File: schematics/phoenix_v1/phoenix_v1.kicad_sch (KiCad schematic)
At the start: 18 parts, among them J1 Screw_Terminal_01x02, J2 Conn_01x09_Socket, SW1 RotaryEncoder_Switch, U1 HHG1D-1, U2 ESP32-S3-DevKitC, U3 NHD-C0220BIZ

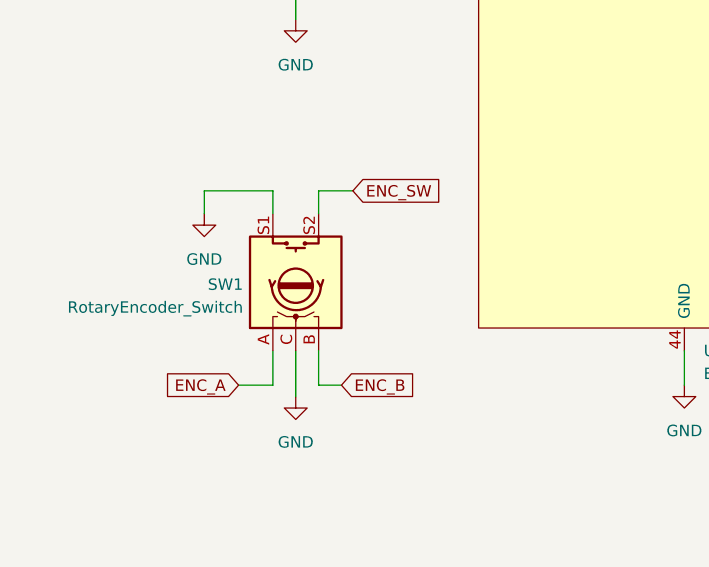
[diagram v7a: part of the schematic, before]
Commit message: fix encoder footprint and label mismatch
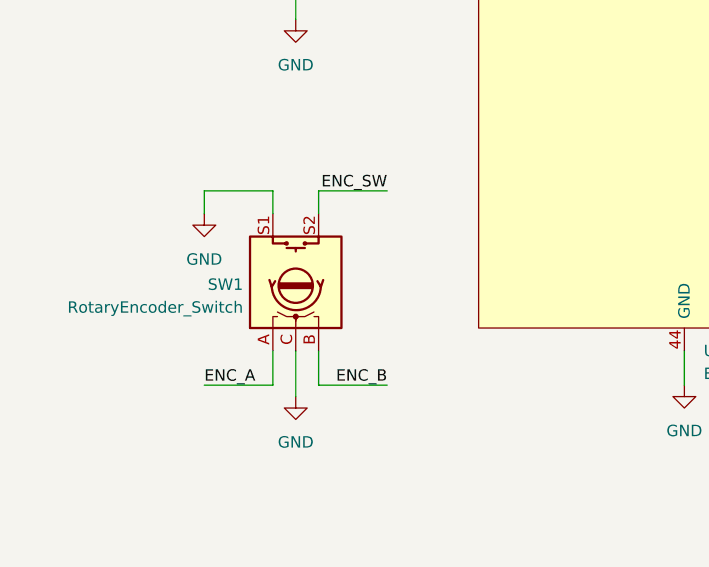
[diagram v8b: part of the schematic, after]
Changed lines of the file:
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@@
-	(wire
-		(pts
-			(xy 48.26 140.97) (xy 44.45 140.97)
-		)
-		(stroke
-			(width 0)
-			(type default)
-		)
-	)
 	(wire
 		(pts
@@
 	(wire
 		(pts
-			(xy 53.34 119.38) (xy 57.15 119.38)
+			(xy 53.34 119.38) (xy 60.96 119.38)
 		)
 		(stroke
@@
 	(wire
 		(pts
-			(xy 53.34 140.97) (xy 55.88 140.97)
+			(xy 53.34 140.97) (xy 60.96 140.97)
 		)
 		(stroke
@@
 		(pts
 			(xy 119.38 132.08) (xy 123.19 132.08)
+		)
+		(stroke
+			(width 0)
+			(type default)
+		)
+	)
+	(wire
+		(pts
+			(xy 40.64 140.97) (xy 48.26 140.97)
 		)
 		(stroke
@@
 		)
 	)
+	(label "ENC_SW"
+		(at 60.96 119.38 180)
+		(effects
+			(font
+				(size 1.27 1.27)
+			)
+			(justify right bottom)
+		)
+	)
 	(label "SCL"
 		(at 146.05 41.91 0)
@@
 		)
 	)
+	(label "ENC_B"
+		(at 60.96 140.97 180)
+		(effects
+			(font
+				(size 1.27 1.27)
+			)
+			(justify right bottom)
+		)
+	)
 	(label "~{FAULT}"
 		(at 116.84 160.02 0)
@@
 		)
 	)
-	(global_label "ENC_SW"
-		(shape input)
-		(at 57.15 119.38 0)
-		(fields_autoplaced yes)
-		(effects
-			(font
-				(size 1.27 1.27)
-			)
-			(justify left)
-		)
-		(property "Intersheetrefs" "${INTERSHEET_REFS}"
-			(at 67.5132 119.38 0)
-			(effects
-				(font
-					(size 1.27 1.27)
-				)
-				(justify left)
-				(hide yes)
-			)
-		)
-	)
-	(global_label "ENC_A"
-		(shape input)
-		(at 44.45 140.97 180)
-		(fields_autoplaced yes)
-		(effects
-			(font
-				(size 1.27 1.27)
-			)
-			(justify right)
-		)
-		(property "Intersheetrefs" "${INTERSHEET_REFS}"
-			(at 35.6591 140.97 0)
-			(effects
-				(font
-					(size 1.27 1.27)
-				)
-				(justify right)
-				(hide yes)
-			)
+	(label "ENC_A"
+		(at 40.64 140.97 0)
+		(effects
+			(font
+				(size 1.27 1.27)
+			)
+			(justify left bottom)
 		)
 	)
@@
 			(effects
 				(font
-					(size 1.27 1.27)
-				)
-				(justify left)
-				(hide yes)
-			)
-		)
-	)
-	(global_label "ENC_B"
-		(shape input)
-		(at 55.88 140.97 0)
-		(fields_autoplaced yes)
-		(effects
-			(font
-				(size 1.27 1.27)
-			)
-			(justify left)
-		)
-		(property "Intersheetrefs" "${INTERSHEET_REFS}"
-			(at 64.8523 140.97 0)
-			(effects
-				(font
